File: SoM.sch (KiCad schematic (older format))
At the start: 7 parts, among them U8 SA800U-WF

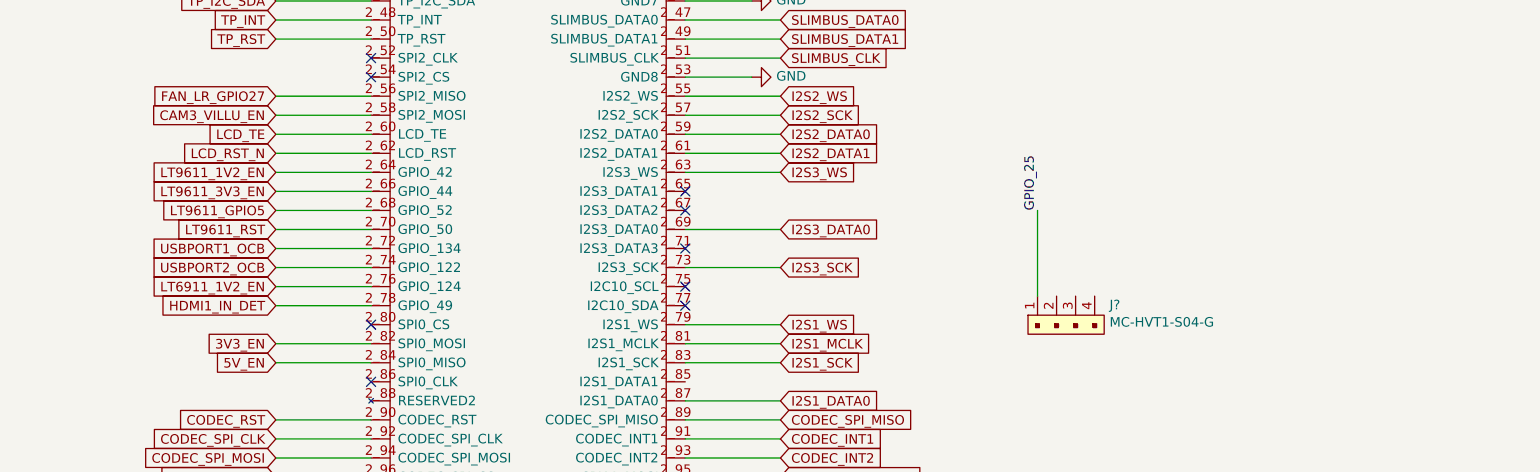
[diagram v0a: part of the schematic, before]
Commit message: finished gpios
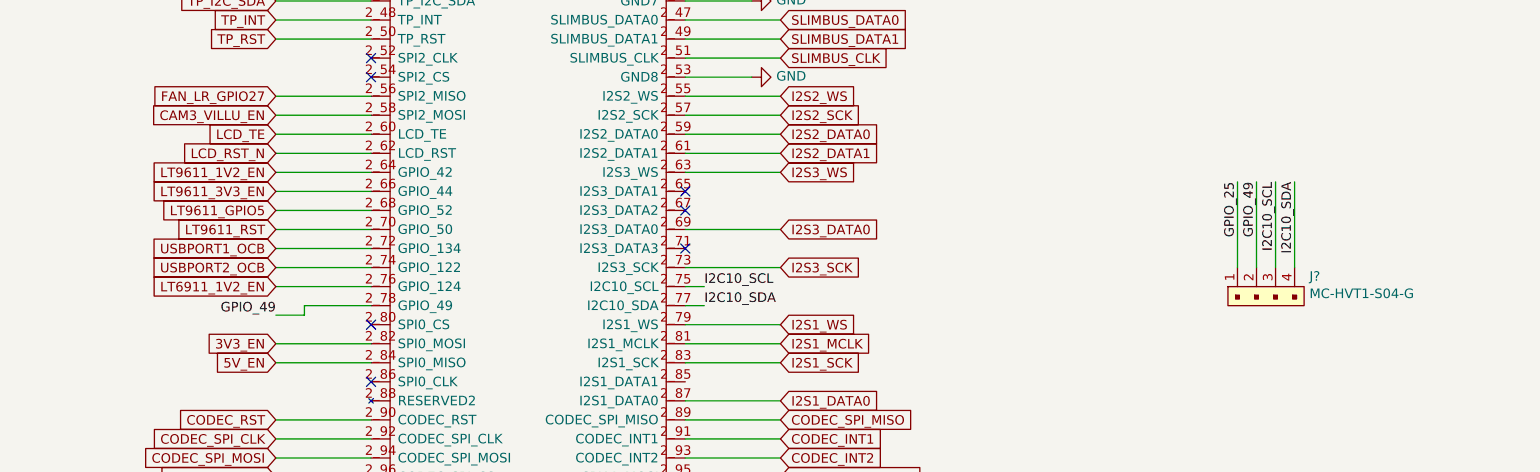
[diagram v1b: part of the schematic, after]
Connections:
- net HDMI1_IN_DET is gone; now on net GPIO_49: U8.2_78 (GPIO_49)
- net I2C10_SCL: now reaches U8.2_75 (I2C10_SCL)
- net I2C10_SCL: now also J?.3
- net I2C10_SDA: now reaches U8.2_77 (I2C10_SDA)
- net I2C10_SDA: now also J?.4
- net GPIO_49: now reaches J?.2
- no-connect marks 40 -> 38
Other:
- moved on the sheet: J?
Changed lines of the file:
@@
 L antmicroRectangularConnectorsHeadersMalePins:MC-HVT1-S04-G J?
 U 1 1 61E93EA5
-P 11600 5400
-F 0 "J?" H 11978 5504 50  0000 L CNN
-F 1 "MC-HVT1-S04-G" H 11978 5413 50  0000 L CNN
-F 2 "antmicro-footprints:PinHeader_1x4_P1.27mm_Drill.7mm" H 11800 5700 60  0001 L CNN
-F 3 "http://www.farnell.com/datasheets/2605295.pdf" H 11800 5800 60  0001 L CNN
-F 4 "MC-HVT1-S04-G" H 11800 5900 60  0001 L CNN "MPN"
-F 5 "Multicomp" H 11800 6000 60  0001 L CNN "Manufacturer"
-	1    11600 5400
+P 12650 5250
+F 0 "J?" H 13028 5354 50  0000 L CNN
+F 1 "MC-HVT1-S04-G" H 13028 5263 50  0000 L CNN
+F 2 "antmicro-footprints:PinHeader_1x4_P1.27mm_Drill.7mm" H 12850 5550 60  0001 L CNN
+F 3 "http://www.farnell.com/datasheets/2605295.pdf" H 12850 5650 60  0001 L CNN
+F 4 "MC-HVT1-S04-G" H 12850 5750 60  0001 L CNN "MPN"
+F 5 "Multicomp" H 12850 5850 60  0001 L CNN "Manufacturer"
+	1    12650 5250
 	1    0    0    -1
 $EndComp
@@
 Text GLabel 7600 5200 0    50   Input ~ 0
 LT6911_1V2_EN
-Text GLabel 7600 5300 0    50   Input ~ 0
-HDMI1_IN_DET
 NoConn ~ 8100 5400
 Text GLabel 7600 5500 0    50   Input ~ 0
@@
 Wire Wire Line
 	7600 5500 8100 5500
-Wire Wire Line
-	8100 5300 7600 5300
 Wire Wire Line
 	7600 5200 8100 5200
@@
 Wire Wire Line
 	10250 5400 9750 5400
-NoConn ~ 9750 5300
-NoConn ~ 9750 5200
 Wire Wire Line
 	10250 5100 9750 5100
@@
 	11800 8050 11800 8350
 Wire Wire Line
-	11600 5250 11600 4800
-Text Label 11600 4800 1    50   ~ 0
+	12650 5100 12650 4650
+Text Label 12650 4650 3    50   ~ 0
 GPIO_25
+Text Label 7600 5350 2    50   ~ 0
+GPIO_49
+Wire Wire Line
+	8100 5300 7750 5300
+Wire Wire Line
+	7750 5300 7750 5350
+Wire Wire Line
+	7750 5350 7600 5350
+Text Label 12750 4650 3    50   ~ 0
+GPIO_49
+Wire Wire Line
+	12750 5100 12750 4650
+Wire Wire Line
+	12850 5100 12850 4650
+Wire Wire Line
+	12950 5100 12950 4650
+Text Label 9850 5200 0    50   ~ 0
+I2C10_SCL
+Text Label 9850 5300 0    50   ~ 0
+I2C10_SDA
+Wire Wire Line
+	9850 5300 9750 5300
+Wire Wire Line
+	9750 5200 9850 5200
+Text Label 12850 4650 3    50   ~ 0
+I2C10_SCL
+Text Label 12950 4650 3    50   ~ 0
+I2C10_SDA
 $EndSCHEMATC

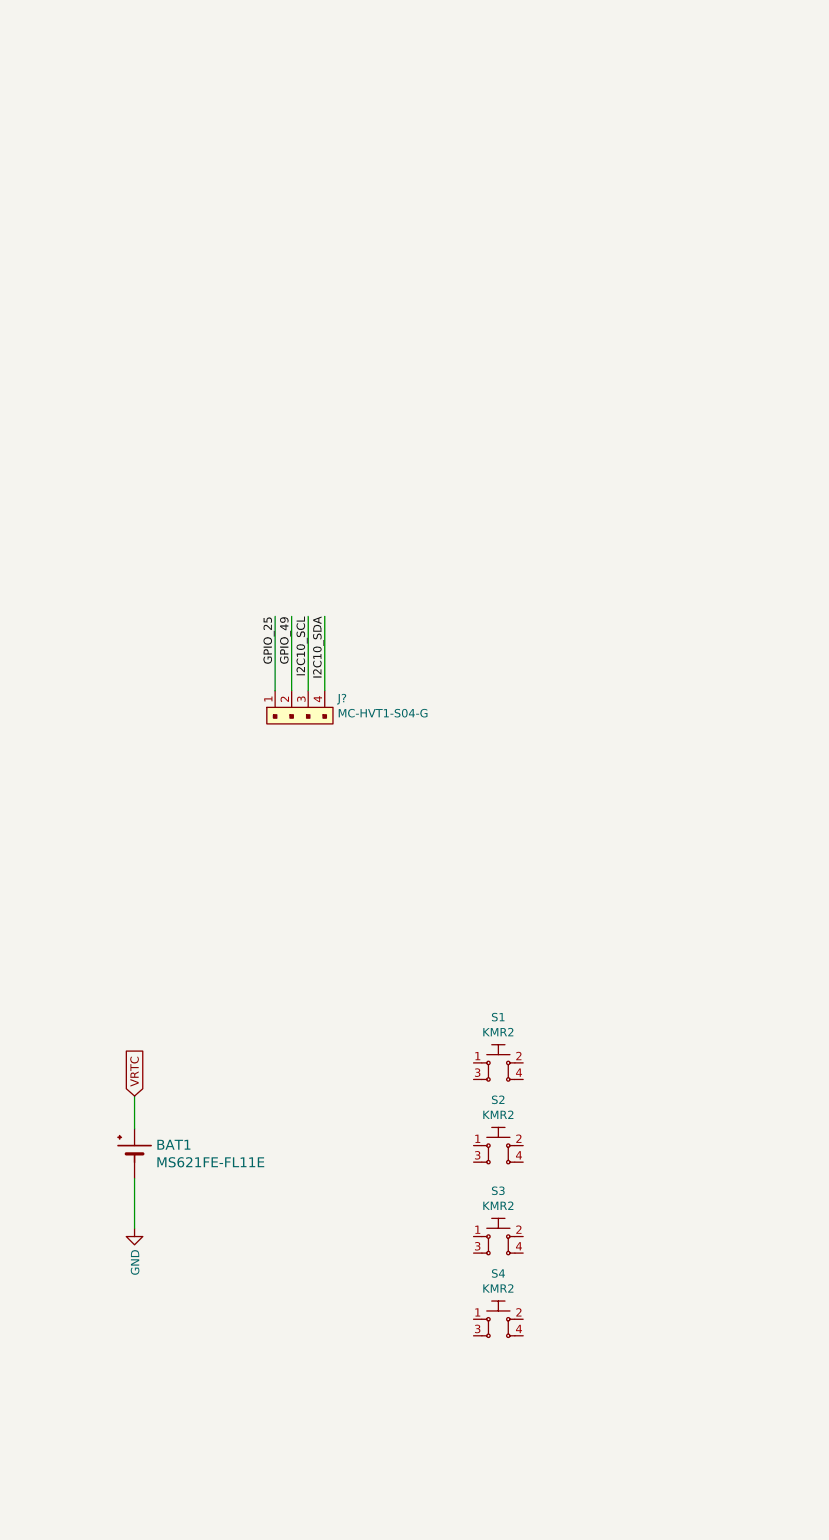
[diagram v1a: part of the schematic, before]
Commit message: fixed TVS diodes for buttons and USB
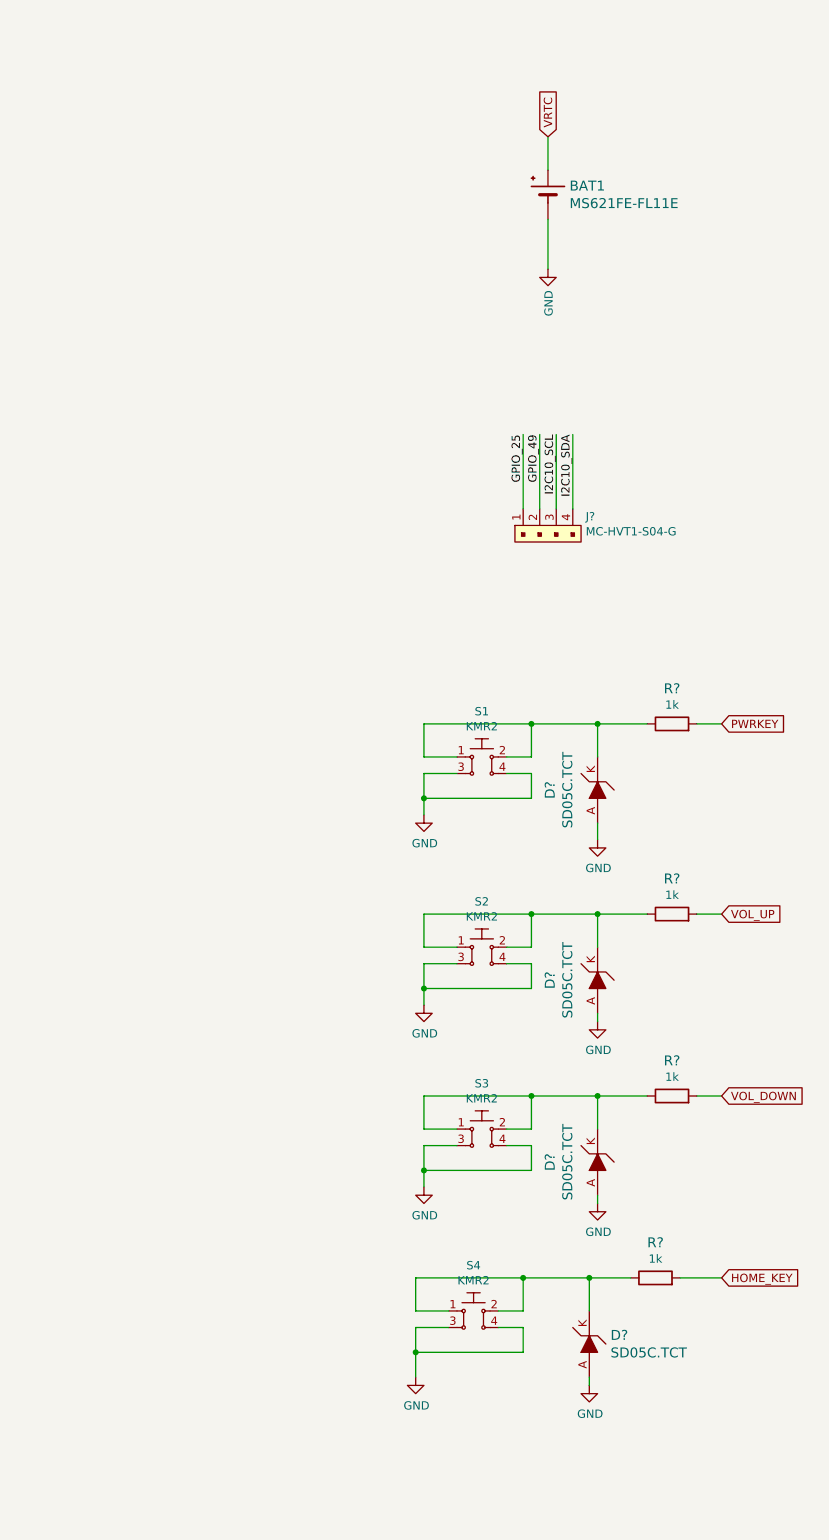
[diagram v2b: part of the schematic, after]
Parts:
- added D? (x4): SD05C.TCT, antmicro-footprints:SOD-323-SD05, symbol antmicroTVSDiodes:SD05C.TCT
- added R? (x4): R_1k_0402, antmicro-footprints:0402-res, symbol antmicroResistors0402:R_1k_0402
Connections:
- net GND: now also S1.3, S1.4, S2.3, S2.4, S3.3, S3.4, S4.3, S4.4, D?.A, D?.A, D?.A, D?.A
- net HOME_KEY: now also R?.2
- net PWRKEY: now also R?.2
- net VOL_DOWN: now also R?.2
- net VOL_UP: now also R?.2
- net at S1.1: now also S1.2, D?.K, R?.1
- net at S2.1: now also S2.2, D?.K, R?.1
- net at S3.1: now also S3.2, D?.K, R?.1
- net at S4.1: now also S4.2, D?.K, R?.1
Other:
- moved on the sheet: BAT1, J?, S1, S2, S3, S4

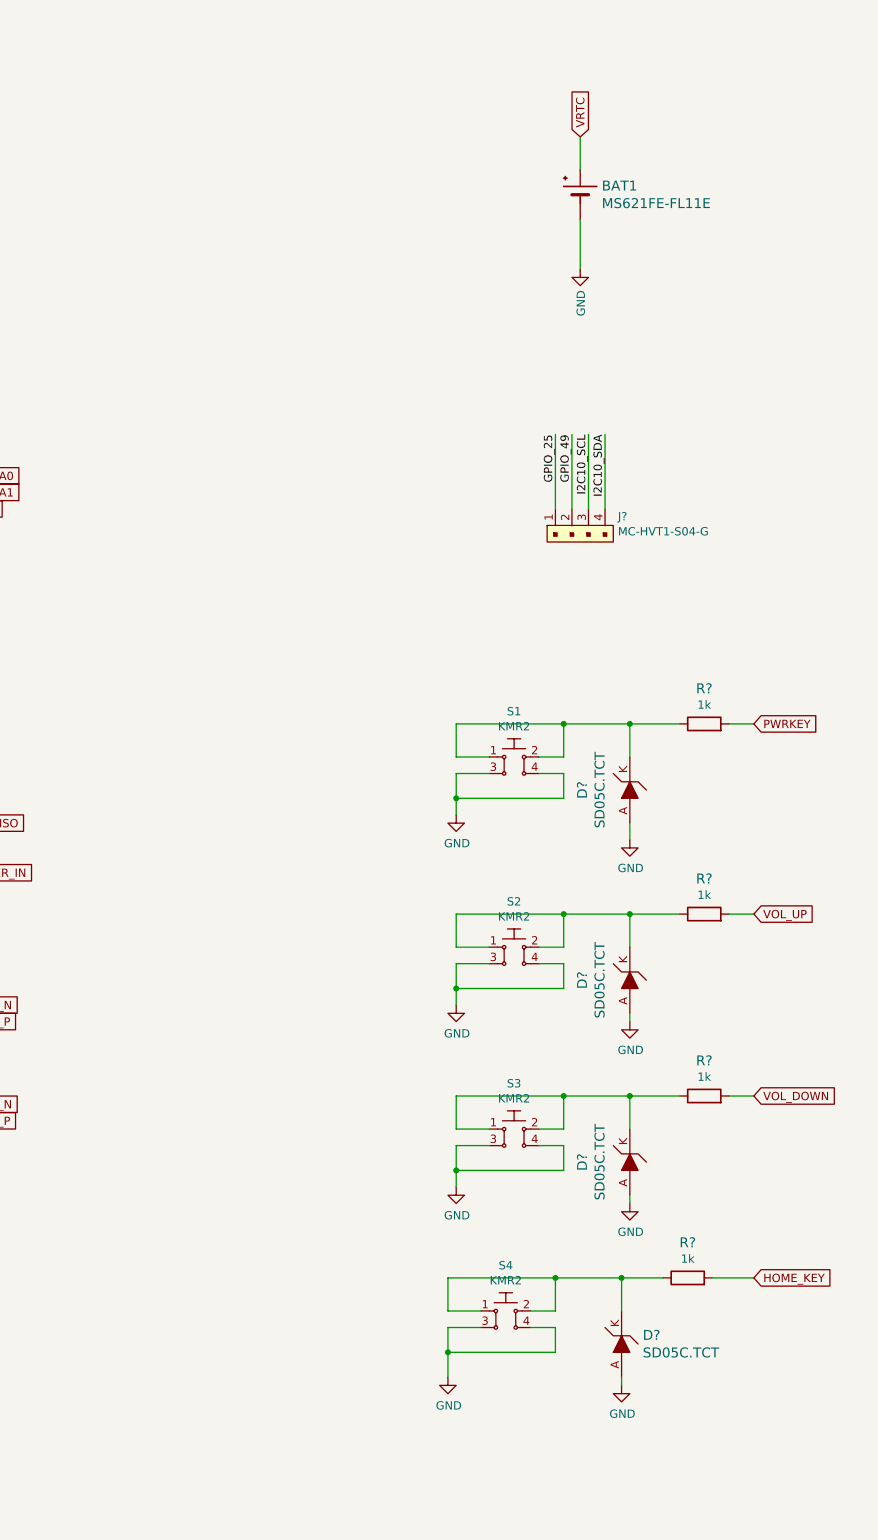
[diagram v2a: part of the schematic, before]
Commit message: changed tvs diodes to ones with smaller wpr voltage and in array
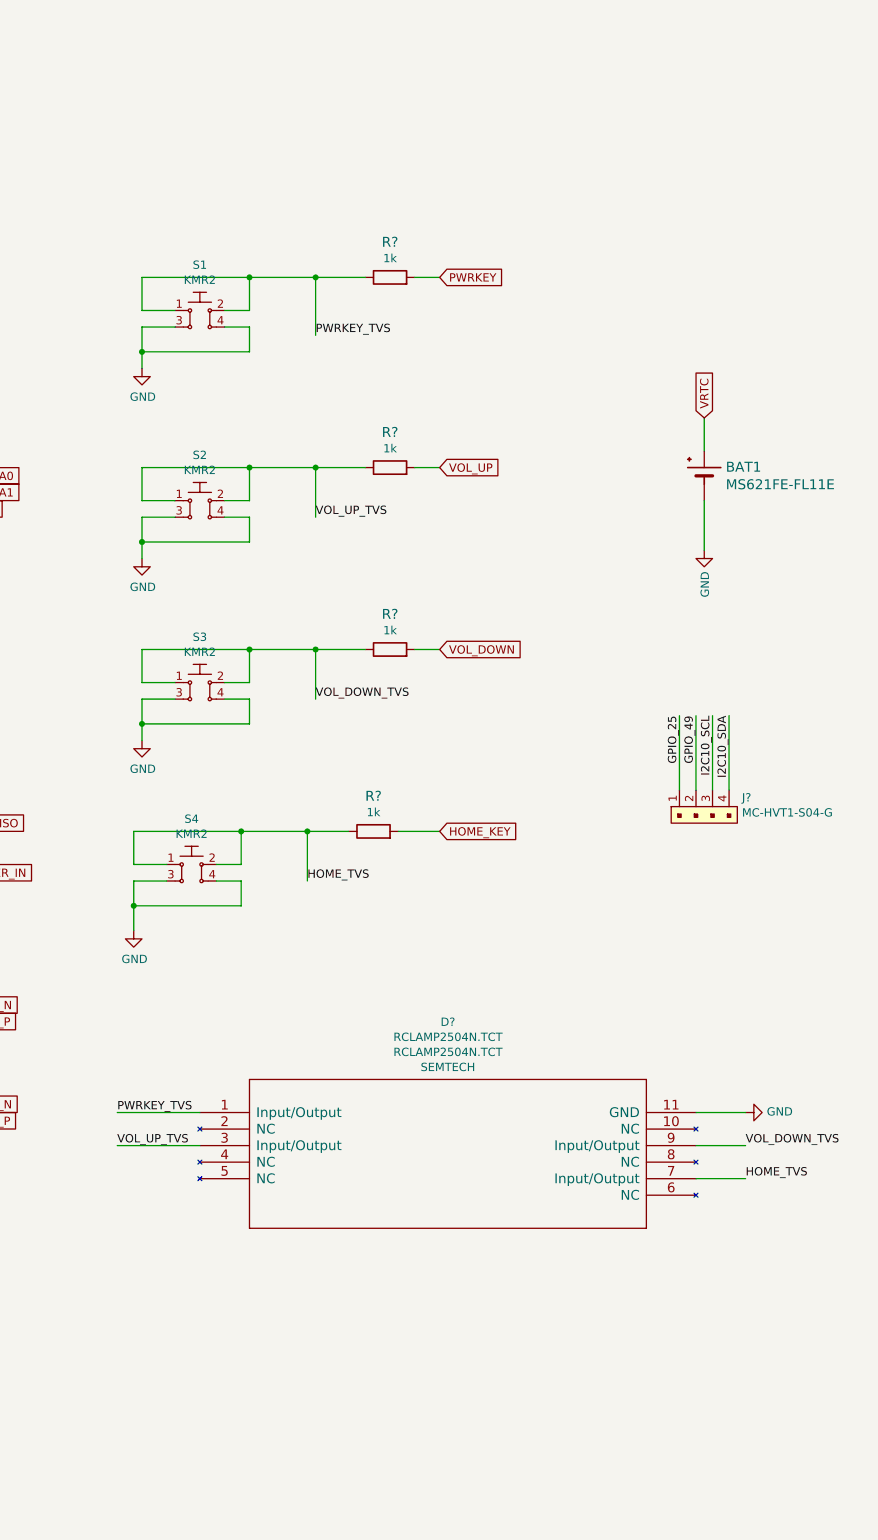
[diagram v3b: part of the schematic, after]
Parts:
- removed D? (x4): SD05C.TCT, antmicro-footprints:SOD-323-SD05, symbol antmicroTVSDiodes:SD05C.TCT
- added D?: RCLAMP2504N.TCT, antmicro-footprints:RCLAMP2504N.TCT, symbol antmicroTVSDiodes:RCLAMP2504N.TCT
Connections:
- net GND: now also D?.11 (GND)
- net PWRKEY_TVS: now reaches R?.1, S1.1, S1.2
- net PWRKEY_TVS: now also D?.1 (Input/Output)
- net VOL_UP_TVS: now reaches R?.1, S2.1, S2.2
- net VOL_UP_TVS: now also D?.3 (Input/Output)
- net VOL_DOWN_TVS: now reaches R?.1, S3.1, S3.2
- net VOL_DOWN_TVS: now also D?.9 (Input/Output)
- net HOME_TVS: now reaches R?.1, S4.1, S4.2
- net HOME_TVS: now also D?.7 (Input/Output)
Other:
- moved on the sheet: BAT1, J?, R?, S1, S2, S3, S4

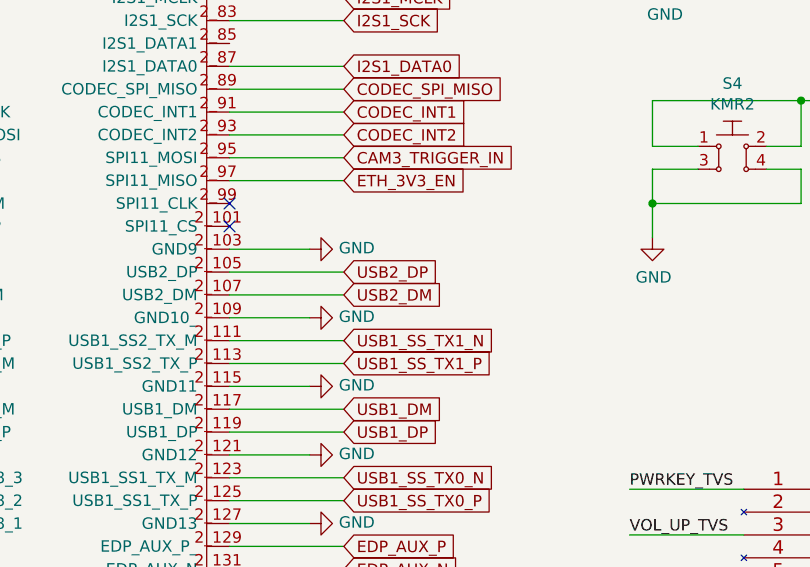
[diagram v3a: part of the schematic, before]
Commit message: connect USB hub - work in progress
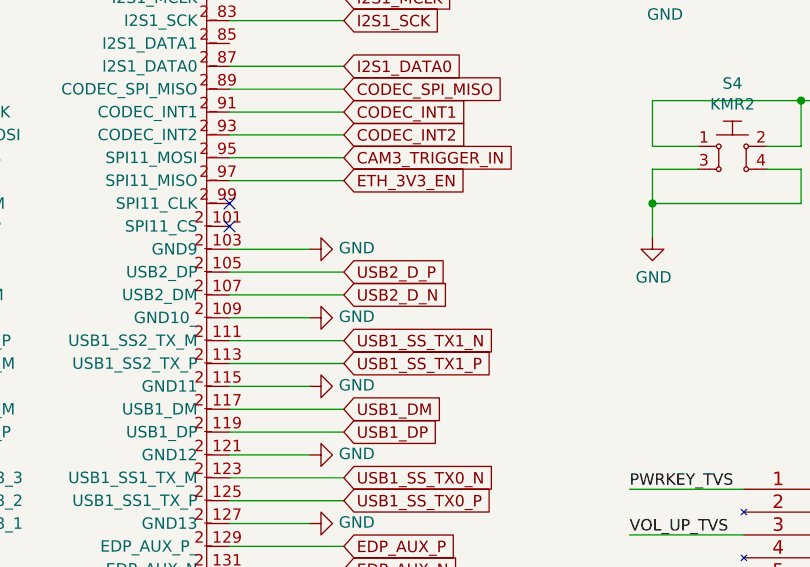
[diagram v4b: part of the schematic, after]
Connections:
- net USB2_DM renamed USB2_D_N
- net USB2_DP renamed USB2_D_P
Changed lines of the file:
@@
 NoConn ~ 9750 6500
 Text GLabel 10250 6700 2    50   Input ~ 0
-USB2_DP
+USB2_D_P
 Text GLabel 10250 6800 2    50   Input ~ 0
-USB2_DM
+USB2_D_N
 Wire Wire Line
 	9750 6900 10100 6900

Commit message: added usb c controller and mux, removed hub
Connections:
- net USB2_FAULT: now reaches U8.1_118 (CAM2_STROBE)
- net USB2_EN: now reaches U8.2_54 (SPI2_CS)
- net USB2_SINK: now reaches U8.2_80 (SPI0_CS)
- no-connect marks 38 -> 35
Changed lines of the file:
@@
 $Descr A3 16535 11693
 encoding utf-8
-Sheet 7 12
+Sheet 7 11
 Title ""
 Date ""
@@
 	1150 7350 1650 7350
 NoConn ~ 1650 7450
-NoConn ~ 1650 7550
 Text GLabel 1150 7650 0    50   Input ~ 0
 CAM1_PWDN
@@
 TP_RST
 NoConn ~ 8100 4000
-NoConn ~ 8100 4100
 Text GLabel 7600 4200 0    50   Input ~ 0
 FAN_LR_GPIO27
@@
 Text GLabel 7600 5200 0    50   Input ~ 0
 LT6911_1V2_EN
-NoConn ~ 8100 5400
 Text GLabel 7600 5500 0    50   Input ~ 0
 3V3_EN
@@
 	1    0    0    -1
 $EndComp
+Text GLabel 7600 4100 0    50   Input ~ 0
+USB2_EN
+Text GLabel 1150 7550 0    50   Input ~ 0
+USB2_FAULT
+Text GLabel 7600 5400 0    50   Input ~ 0
+USB2_SINK
+Wire Wire Line
+	8100 4100 7600 4100
+Wire Wire Line
+	1650 7550 1150 7550
+Wire Wire Line
+	8100 5400 7600 5400
 $EndSCHEMATC

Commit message: changed arrangement of hierarchical sheets
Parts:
- gave numbers to parts that had none: 6
